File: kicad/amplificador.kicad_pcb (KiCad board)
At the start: 2 copper layers, 79 parts, among them J1 Screw_Terminal_01x01, J10 Conn_01x01_Male, J11 Conn_01x01_Male, J12 Conn_01x01_Male, J13 Conn_01x01_Male, J16 Screw_Terminal_01x01, J17 Screw_Terminal_01x01, J18 Conn_01x01_Male, J19 Conn_01x01_Male, J2 Conn_01x01_Male, J3 Conn_01x01_Male, J4 Conn_01x01_Male, J5 Conn_01x01_Male, J6 Conn_01x01_Male, J7 Screw_Terminal_01x01, J8 Screw_Terminal_01x01, J9 Conn_01x01_Male, Q1 MPSA92, Q10 MPSA42, Q11 BD135, Q12 BD136, Q13 BD135, Q14 BD136, Q15 2SD1047, Q16 2SD1047, Q17 2SB817, Q18 2SB817, Q2 MPSA42, Q3 MPSA92, Q4 MPSA42, Q5 MPSA92, Q6 MPSA92, Q7 MPSA42, Q8 MPSA92, Q9 MPSA42, U1 LM385D-1.2, U2 LM385D-1.2

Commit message: How many vias are too many vias?
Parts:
- moved J16 134.6 mm to (68.5, 35.9), turned to 180 degrees
- moved J4 132.7 mm to (65.4, 73.6), turned to 0 degrees
- moved D5 128.5 mm to (77.4, 35.9), turned to 0 degrees
- moved J17 123.2 mm to (245.5, 35.8), turned to 0 degrees
- moved R22 121.9 mm to (70.8, 63.7)
- moved Q12 119.7 mm to (83.4, 52.7)
- moved J19 118.5 mm to (78.7, 91.9), turned to 0 degrees
- moved C7 118.1 mm to (95.8, 60.8), turned to 180 degrees
- moved J7 116.8 mm to (65.8, 124.6), turned to 180 degrees
- moved J1 116.7 mm to (79.0, 100.5), turned to 90 degrees
- moved J9 114.2 mm to (223.7, 103.1)
- moved Q3 113.7 mm to (86.2, 83.6), turned to 270 degrees
- moved C2 113.0 mm to (92.3, 89.8), turned to 90 degrees
- moved R21 112.9 mm to (222.6, 52.6), turned to 90 degrees
- moved R4 111.8 mm to (94.1, 71.6), turned to 90 degrees
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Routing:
- net Net-(C2-Pad2): track 0.00 -> 277.3 mm, vias 0 -> 4
- net Net-(C8-Pad1): track 0.00 -> 243.0 mm, vias 0 -> 3
- net Net-(J13-Pad1): track 0.00 -> 163.9 mm, vias 0 -> 2
- net GND: track 0.00 -> 136.4 mm, vias 0 -> 3
- net Net-(C6-Pad1): track 0.00 -> 121.8 mm, vias 0 -> 2
- net Net-(J12-Pad1): track 0.00 -> 117.2 mm, vias 0 -> 3
- net Net-(C5-Pad1): track 0.00 -> 108.5 mm, vias 0 -> 1
- net Net-(Q8-Pad2): track 0.00 -> 96.0 mm, vias 0 -> 1
- net Net-(D5-Pad2): track 0.00 -> 92.6 mm, vias 0 -> 1
- net Net-(D4-Pad2): track 0.00 -> 76.6 mm
- net Net-(C6-Pad2): track 0.00 -> 73.1 mm, vias 0 -> 1
- net Net-(D6-Pad1): track 0.00 -> 65.9 mm, vias 0 -> 1
- net Net-(Q11-Pad1): track 0.00 -> 63.9 mm, vias 0 -> 2
- net Net-(Q9-Pad2): track 0.00 -> 61.5 mm, vias 0 -> 1
- net Net-(D3-Pad1): track 0.00 -> 60.8 mm, vias 0 -> 1
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- added copper zone on B.Cu, net GND
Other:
- board outline added: 202 x 100 mm

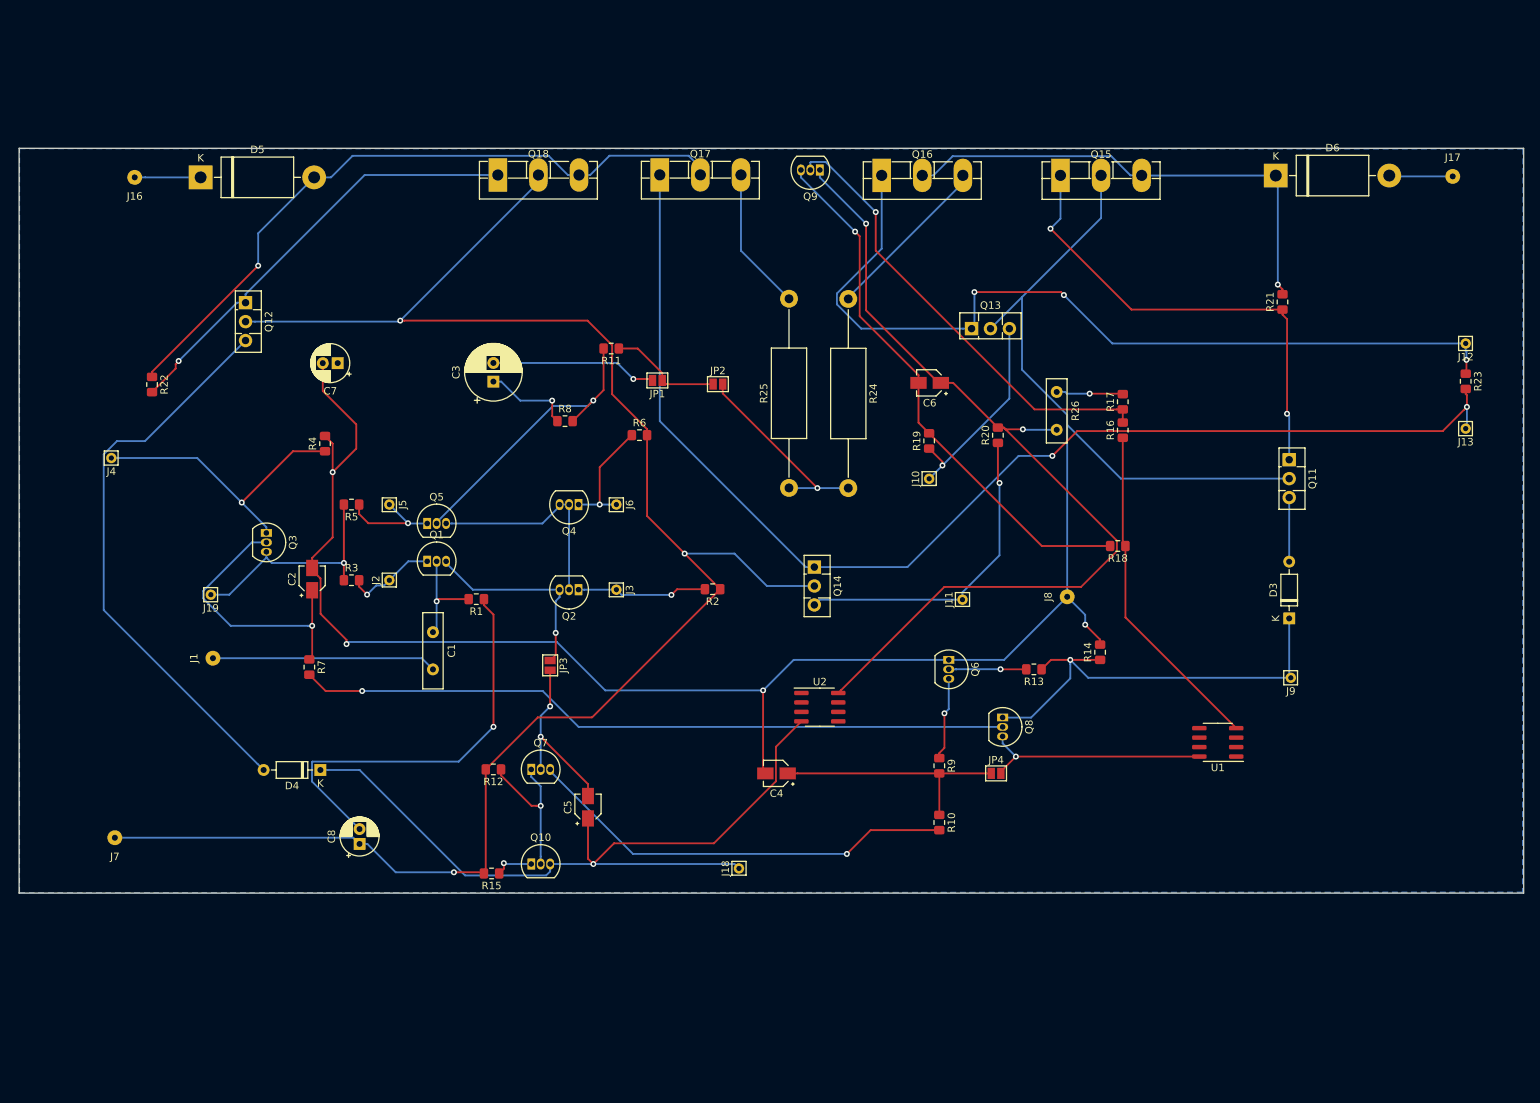
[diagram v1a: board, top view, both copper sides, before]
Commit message: PCB DRC actualizado
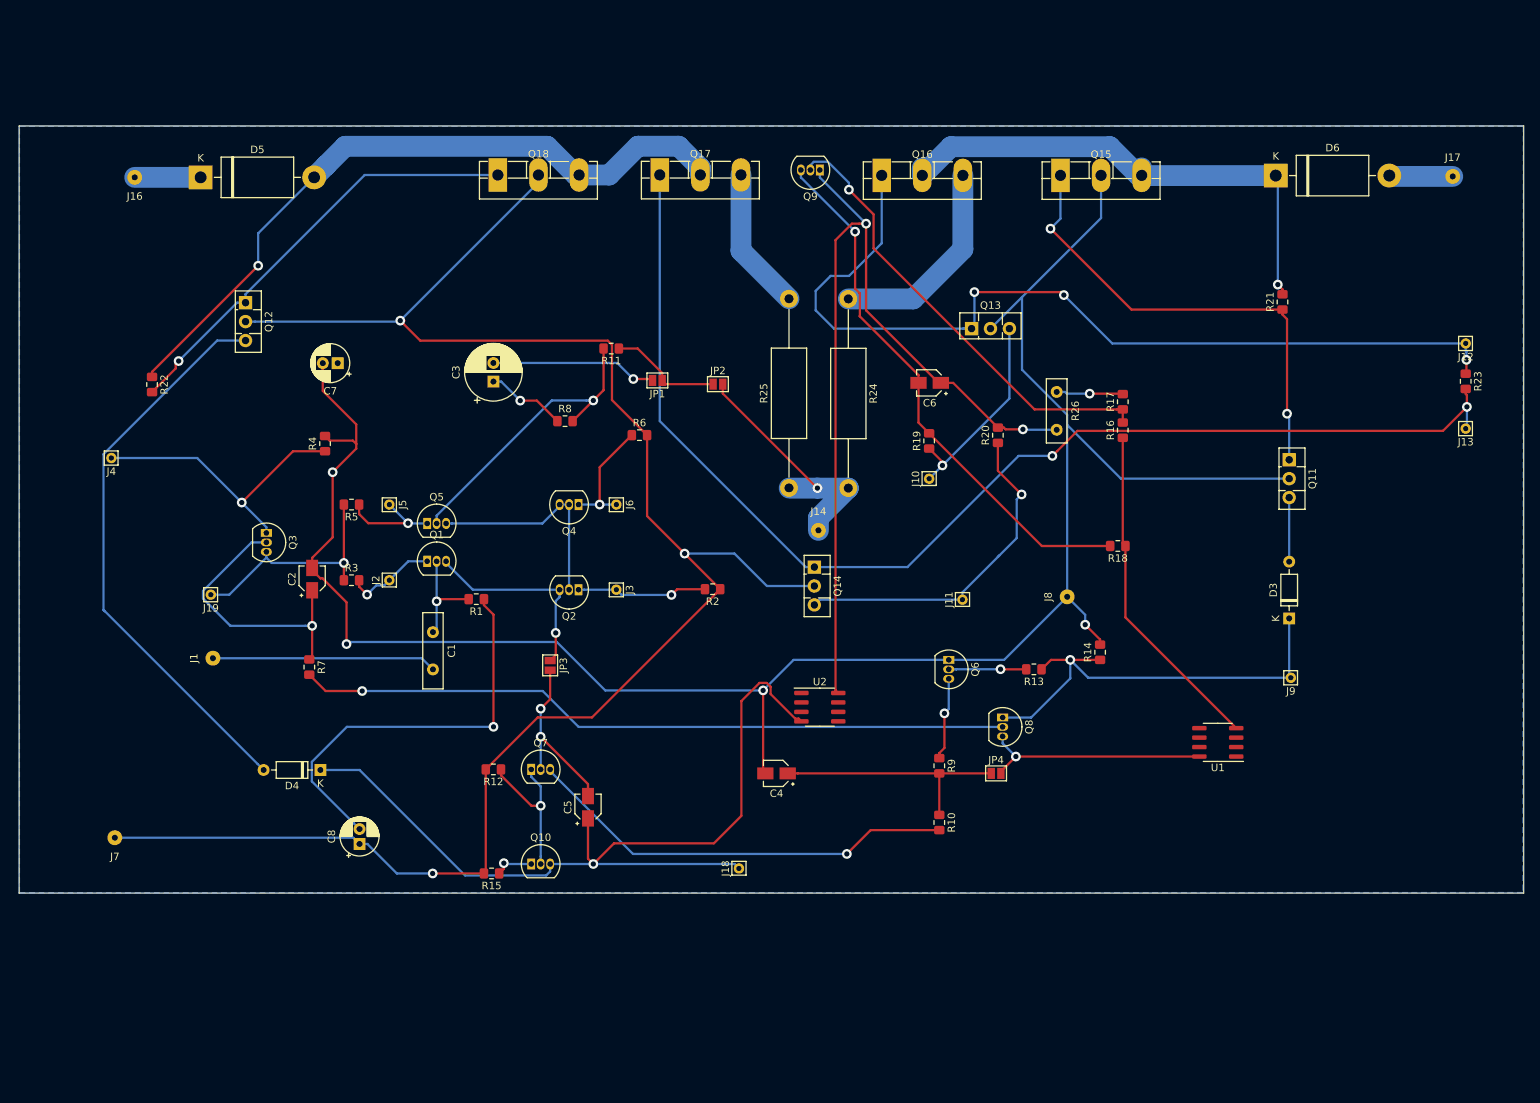
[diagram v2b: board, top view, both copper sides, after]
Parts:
- added J14: Screw_Terminal_01x01, Connector_Wire:SolderWirePad_1x01_Drill0.8mm, F.Cu at (160.3, 83.3)
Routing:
- net Net-(C5-Pad1): track 108.5 -> 119.7 mm
- net Net-(J14-Pad1): track 27.2 -> 34.5 mm
- net Net-(J12-Pad1): track 117.2 -> 124.3 mm
- net Net-(Q16-Pad3): track 23.0 -> 29.3 mm
- net Net-(D5-Pad2): track 92.6 -> 95.7 mm
- net Net-(D6-Pad1): track 65.9 -> 69.0 mm
- net Net-(J11-Pad1): track 43.4 -> 46.1 mm
- net Net-(C6-Pad1): track 121.8 -> 119.6 mm
- net Net-(C3-Pad1): track 12.0 -> 10.8 mm
- net Net-(C8-Pad1): track 243.0 -> 243.8 mm
- net Net-(Q5-Pad2): track 39.4 -> 40.1 mm
- net Net-(C2-Pad1): track 37.8 -> 38.4 mm
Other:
- board size 202 x 100 mm -> 202 x 103 mm
- net class Default: trace_width 0.25 -> 0.3048; via_dia 0.8 -> 1.309624; via_drill 0.4 -> 0.700024
- rule trace_min: 0.2 -> 0.3048
- rule via_min_size: 0.4 -> 1.309624

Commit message: PCB versión 1.0
Planos de alimentación, ancho de pistas y nuevos pines GND.
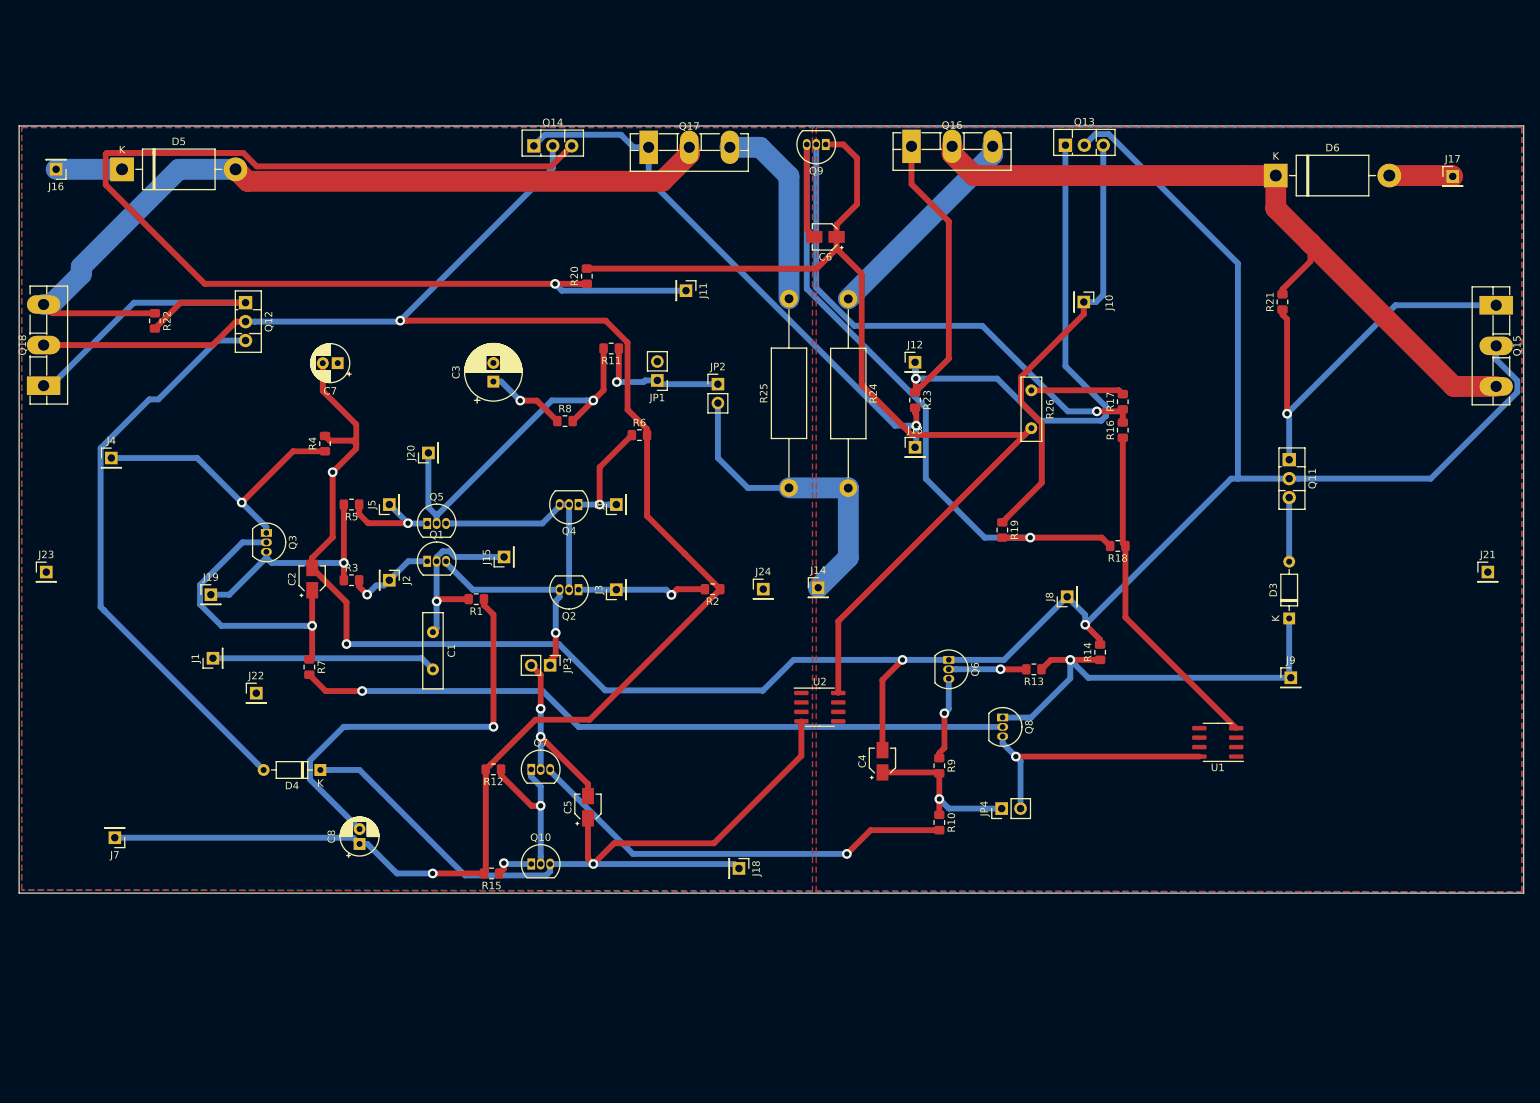
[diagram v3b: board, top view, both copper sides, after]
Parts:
- added J15: Conn_01x01_Male, Connector_PinHeader_2.54mm:PinHeader_1x01_P2.54mm_Vertical, F.Cu at (118.1, 86.9)
- added J20: Conn_01x01_Male, Connector_PinHeader_2.54mm:PinHeader_1x01_P2.54mm_Vertical, F.Cu at (108.0, 72.9)
- added J21: Screw_Terminal_01x01, Connector_PinHeader_2.54mm:PinHeader_1x01_P2.54mm_Vertical, F.Cu at (250.2, 88.9)
- added J22: Screw_Terminal_01x01, Connector_PinHeader_2.54mm:PinHeader_1x01_P2.54mm_Vertical, F.Cu at (84.8, 105.2)
- added J23: Screw_Terminal_01x01, Connector_PinHeader_2.54mm:PinHeader_1x01_P2.54mm_Vertical, F.Cu at (56.6, 88.9)
- added J24: Screw_Terminal_01x01, Connector_PinHeader_2.54mm:PinHeader_1x01_P2.54mm_Vertical, F.Cu at (152.9, 91.2)
- J1, J14, J16, J17, J7, J8: footprint Connector_Wire:SolderWirePad_1x01_Drill0.8mm -> Connector_PinHeader_2.54mm:PinHeader_1x01_P2.54mm_Vertical
- J10, J11, J12, J13, J18, J19, J2, J3, J4, J5, J6, J9: footprint Connector_Pin:Pin_D0.7mm_L6.5mm_W1.8mm_FlatFork -> Connector_PinHeader_2.54mm:PinHeader_1x01_P2.54mm_Vertical
- JP1, JP2, JP3, JP4: footprint kicad:SolderJumper-2_P1.3mm_Open_Pad1.0x1.5mm -> Connector_PinHeader_2.54mm:PinHeader_1x02_P2.54mm_Vertical
- moved J12 74.0 mm to (173.3, 60.7)
- moved J13 74.0 mm to (173.3, 72.2)
- moved R23 74.0 mm to (173.3, 65.8)
- moved Q14 67.9 mm to (122.1, 31.7), turned to 0 degrees
- moved Q18 67.2 mm to (56.3, 63.9), turned to 90 degrees
- moved Q15 61.0 mm to (251.3, 53.1), turned to 270 degrees
- moved R20 59.2 mm to (129.2, 49.2)
- moved J11 55.7 mm to (142.5, 51.1)
- moved J10 31.5 mm to (195.9, 52.6)
- moved Q13 27.7 mm to (193.5, 31.6)
- moved C6 24.1 mm to (161.3, 43.9)
- moved R19 15.5 mm to (185.0, 83.2), turned to 270 degrees
- moved C4 14.3 mm to (168.9, 114.3), turned to 90 degrees
- moved D5 10.6 mm to (66.8, 34.8)
- moved J16 10.6 mm to (58.0, 34.8)
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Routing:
- net Net-(J11-Pad1): track 46.1 -> 156.7 mm
- net Net-(J13-Pad1): track 163.9 -> 76.1 mm, vias 2 -> 1
- net Net-(C2-Pad2): track 276.8 -> 310.8 mm
- net Net-(J10-Pad1): track 27.6 -> 59.5 mm, vias 1 -> 0
- net Net-(D6-Pad1): track 69.0 -> 98.4 mm, vias 1 -> 0
- net Net-(C6-Pad1): track 119.6 -> 144.8 mm, vias 2 -> 0
- net Net-(C6-Pad2): track 73.1 -> 96.6 mm
- net GND: track 136.5 -> 114.6 mm, vias 3 -> 2
- net Net-(D5-Pad2): track 95.7 -> 113.3 mm, vias 1 -> 0
- net Net-(J12-Pad1): track 124.3 -> 107.9 mm, vias 3 -> 1
- net Net-(C8-Pad1): track 243.8 -> 259.1 mm, vias 3 -> 2
- net Net-(Q12-Pad1): track 59.5 -> 45.3 mm, vias 1 -> 0
- net Net-(C5-Pad1): track 119.7 -> 108.5 mm
- net Net-(C4-Pad1): track 32.9 -> 22.2 mm, vias 0 -> 1
- net Net-(C1-Pad1): track 14.1 -> 24.4 mm
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- added copper zone on F.Cu, net Net-(C2-Pad2)
- added copper zone on F.Cu, net Net-(C8-Pad1)
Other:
- net class Default: trace_width 0.3048 -> 0.7874
- rule trace_min: 0.3048 -> 0.7874

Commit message: Planos de masa separados por etapas
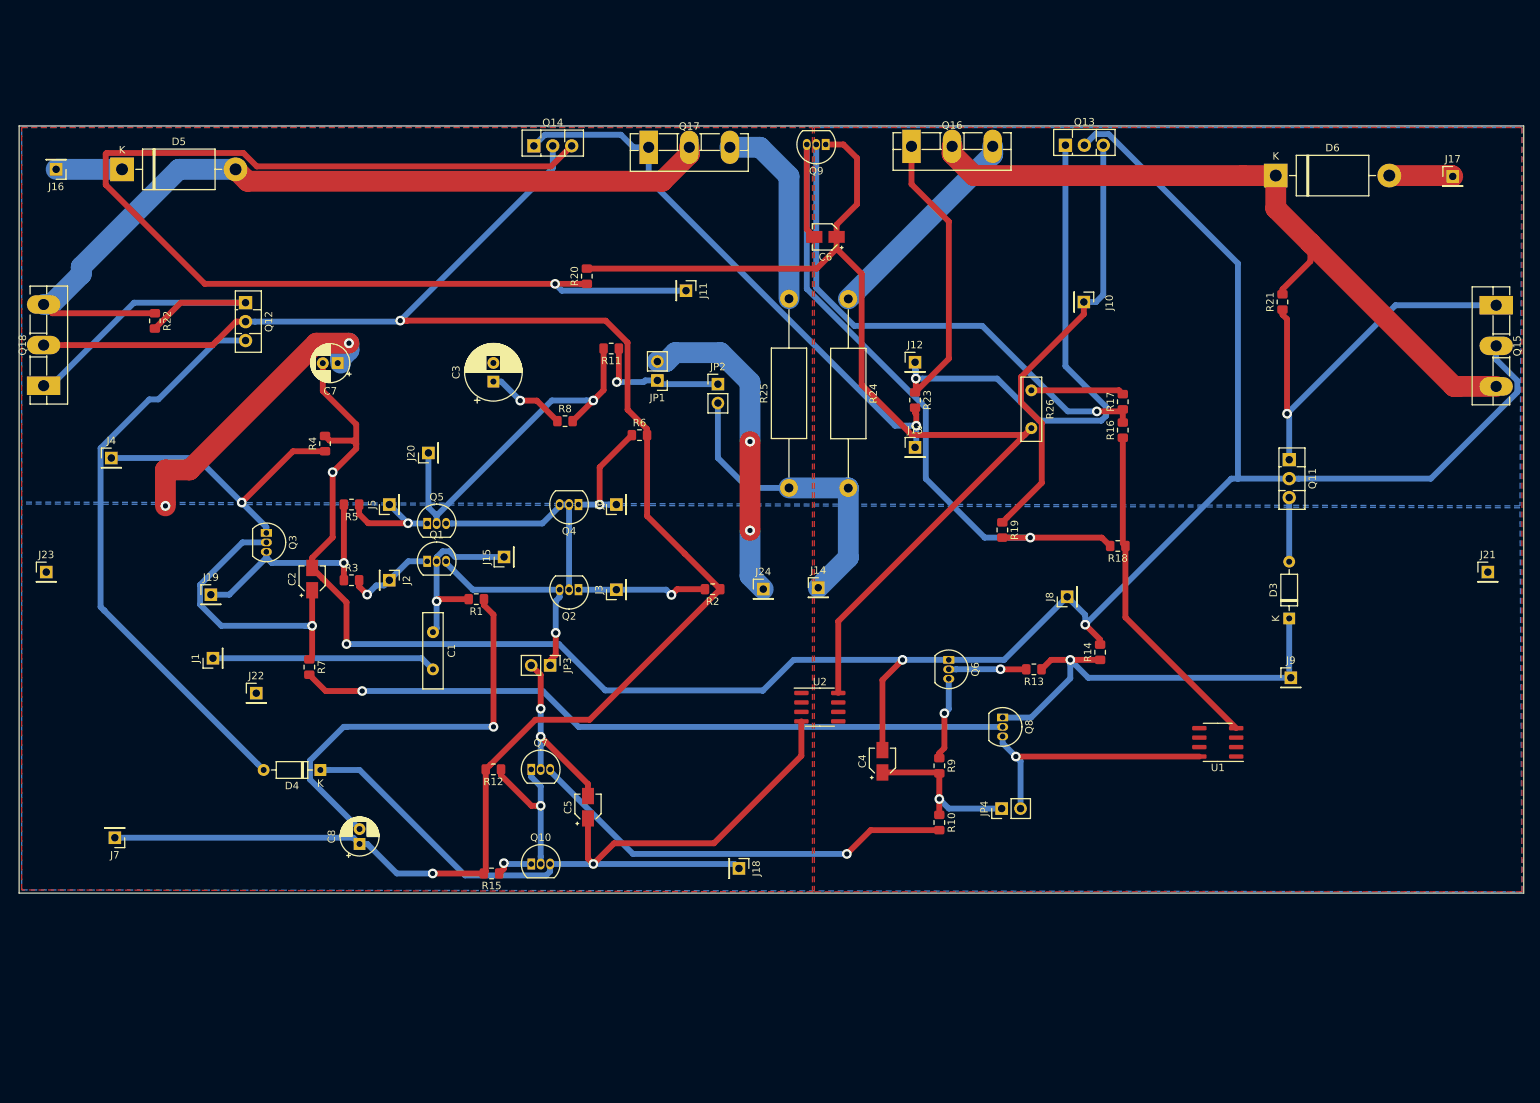
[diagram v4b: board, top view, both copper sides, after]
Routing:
- net GND: track 114.6 -> 197.3 mm, vias 2 -> 6
- removed copper zone on F.Cu, net Net-(C2-Pad2)
